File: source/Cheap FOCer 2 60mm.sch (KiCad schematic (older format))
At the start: 49 parts, among them J1 Conn_01x02, J2 Conn_01x07, J3 Conn_01x03, J6 Conn_01x03, P1 MOTOR1, P2 MOTOR1, P3 MOTOR1, P4 HALL/Encoder

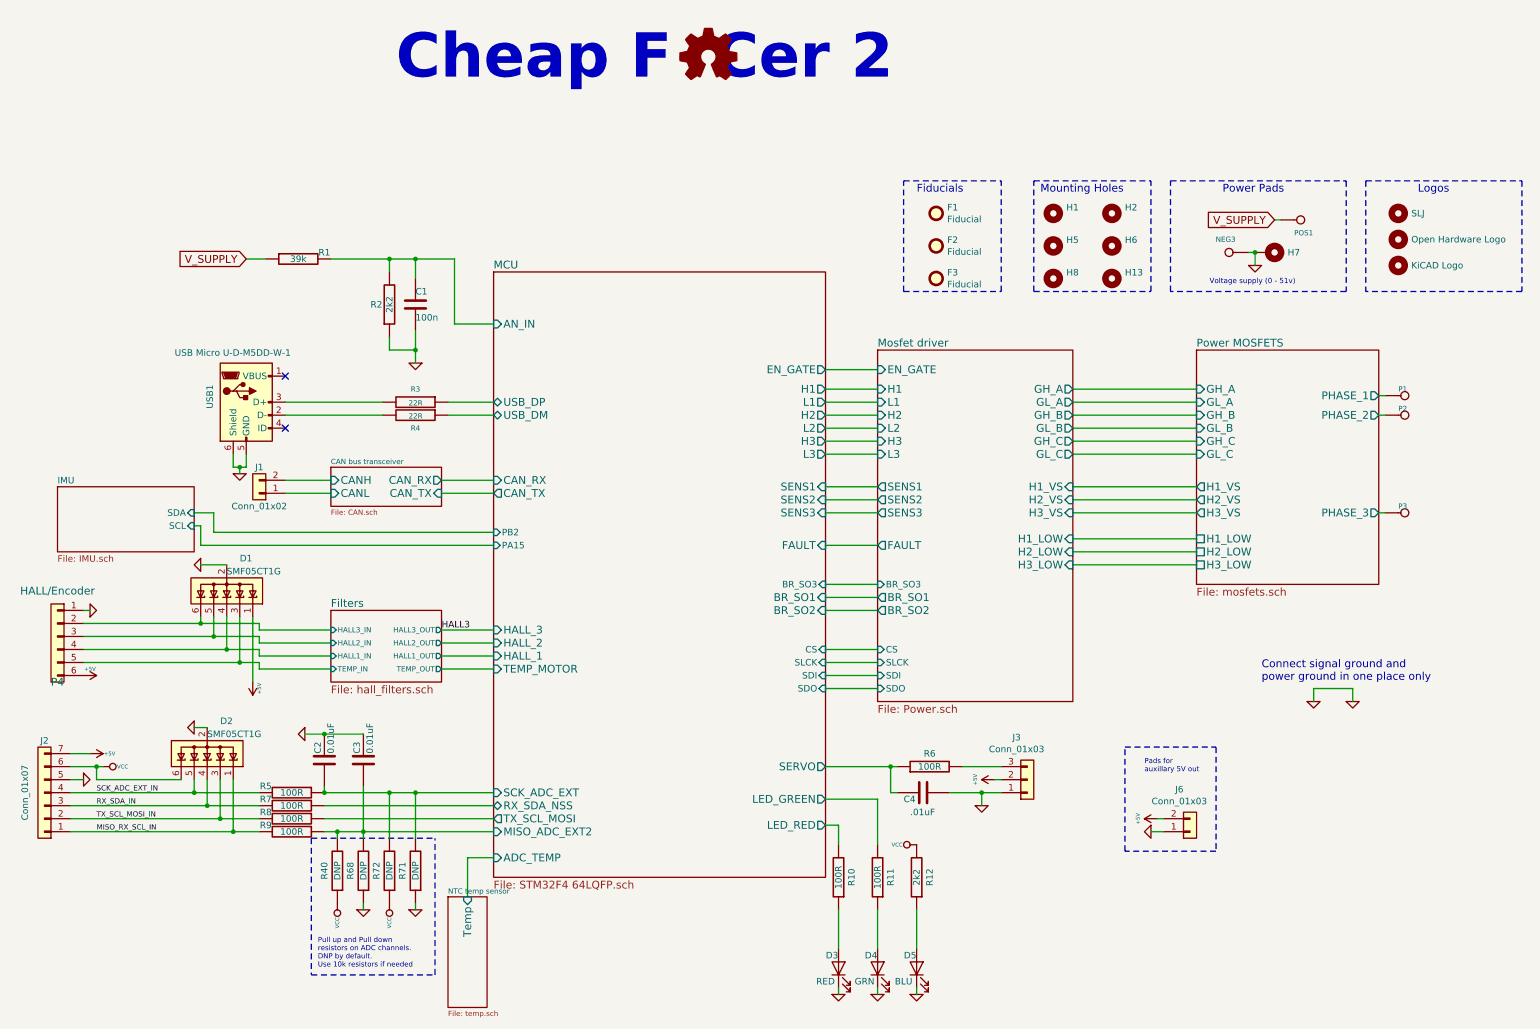
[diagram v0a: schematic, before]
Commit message: started redrawing pcb
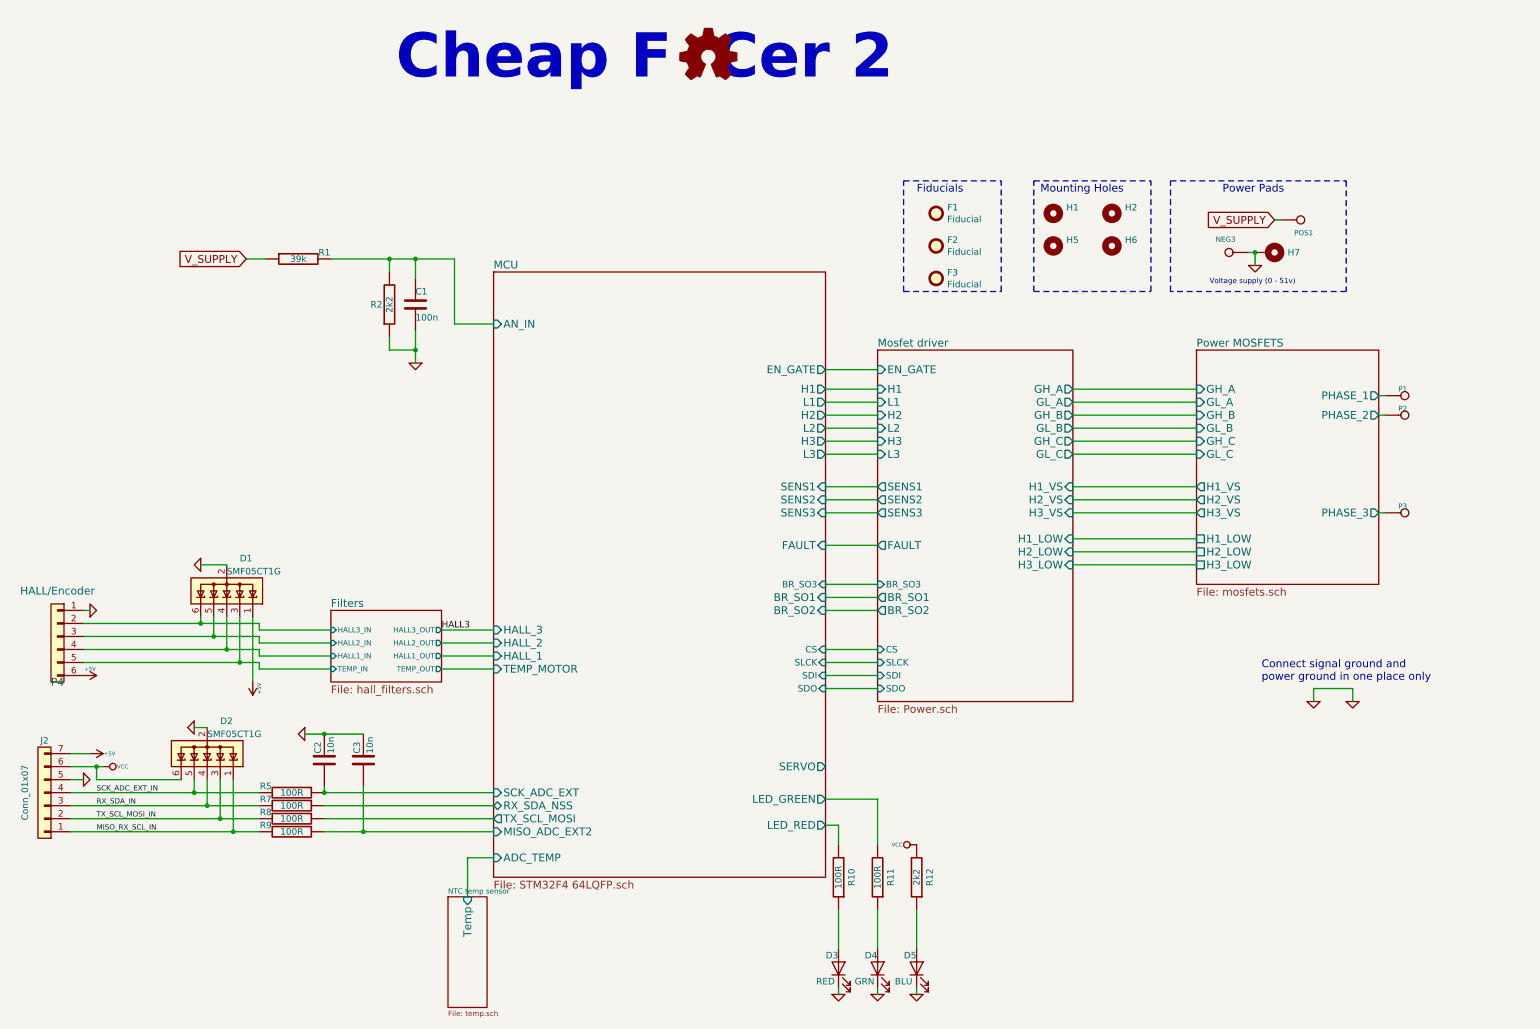
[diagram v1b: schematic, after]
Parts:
- removed C4: .01uF, Capacitor_SMD:C_0603_1608Metric, symbol BLDC_4-rescue:C-RESCUE-BLDC_4
- removed H13, H8: MountingHole, MountingHole:MountingHole_3.2mm_M3_ISO14580_Pad, symbol Mechanical:MountingHole
- removed H3: SLJ, shapes3D:Sam_J, symbol Mechanical:MountingHole
- removed H4: Open Hardware Logo, Symbol:OSHW-Logo2_9.8x8mm_SilkScreen, symbol Mechanical:MountingHole
- removed H9: KiCAD Logo, Symbol:KiCad-Logo2_5mm_SilkScreen, symbol Mechanical:MountingHole
- removed J1: Conn_01x02, Connector_JST:JST_PH_B2B-PH-K_1x02_P2.00mm_Vertical, symbol Connector_Generic:Conn_01x02
- removed J3: Conn_01x03, Connector_JST:JST_PH_B3B-PH-K_1x03_P2.00mm_Vertical, symbol Connector_Generic:Conn_01x03
- removed J6: Conn_01x03, Connector_PinHeader_2.54mm:PinHeader_1x02_P2.54mm_Vertical, symbol Connector_Generic:Conn_01x02
- removed R3, R4: 22R, Resistor_SMD:R_0603_1608Metric, symbol BLDC_4-rescue:R-RESCUE-BLDC_4
- removed R40, R68, R71, R72: DNP, Resistor_SMD:R_0603_1608Metric, symbol BLDC_4-rescue:R-RESCUE-BLDC_4
- removed R6: 100R, Resistor_SMD:R_0603_1608Metric, symbol BLDC_4-rescue:R-RESCUE-BLDC_4
- removed USB1: USB Micro U-D-M5DD-W-1, Connector_USB:USB_Micro-B_Wuerth_614105150721_Vertical, symbol Connector:USB_B_Micro
- C1: footprint Capacitor_SMD:C_0603_1608Metric -> Capacitor_SMD:C_0402_1005Metric
- C2, C3: value 0.01uF -> 10n; footprint Capacitor_SMD:C_0603_1608Metric -> Capacitor_SMD:C_0402_1005Metric
- R1, R10, R11, R12, R2, R5, R7, R8, R9: footprint Resistor_SMD:R_0603_1608Metric -> Resistor_SMD:R_0402_1005Metric
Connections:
- no-connect marks 2 -> 0
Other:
- note removed: "Logos"
- note removed: "Pads for \nauxillary 5V out"
- note removed: "Pull up and Pull down \nresistors on ADC channels. \nDNP by default.\nUse 10k resistors if needed"
